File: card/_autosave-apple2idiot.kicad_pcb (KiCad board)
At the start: 2 copper layers, 167.6 x 77.5 mm, 4 parts, among them J1 CARD EDGE, U1 IDT7132, U2 ESP32-WROOM-32

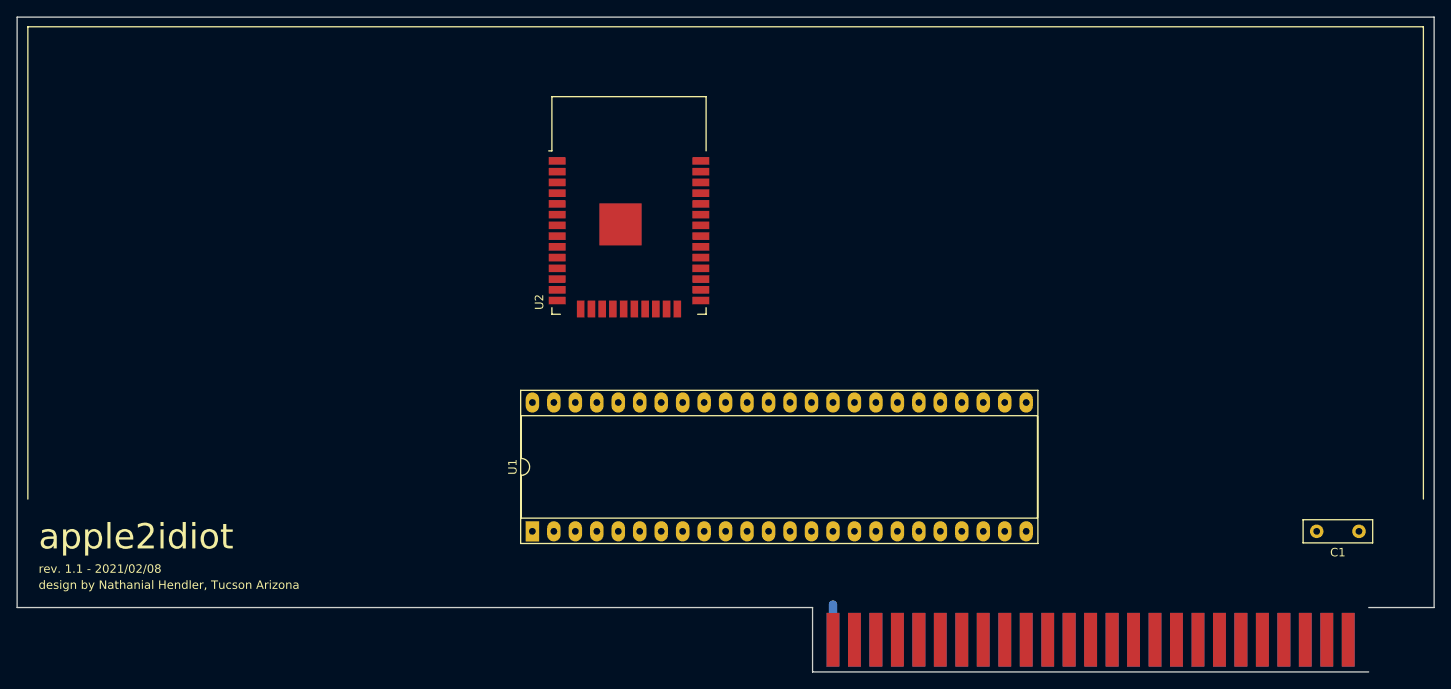
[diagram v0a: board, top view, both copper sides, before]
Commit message: ESP w/ webserver writes to RAM
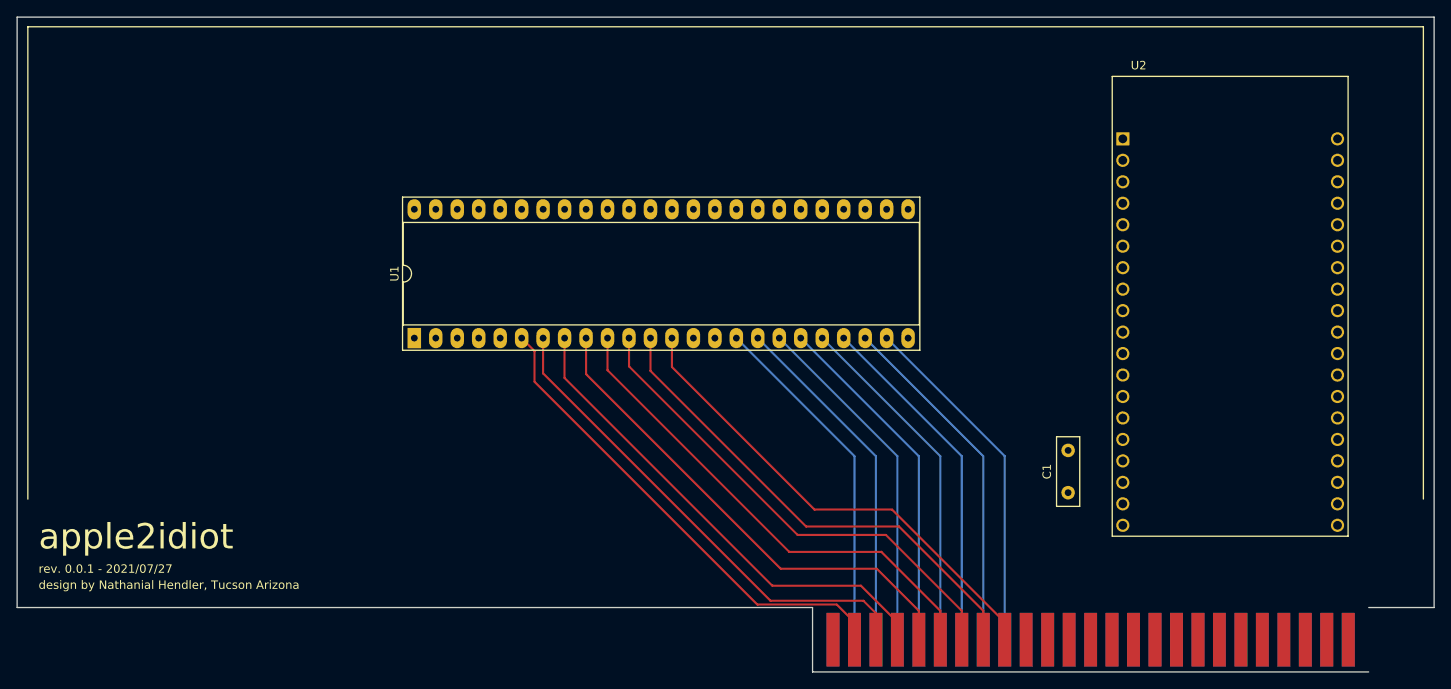
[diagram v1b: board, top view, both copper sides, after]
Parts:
- U2: value ESP32-WROOM-32 -> ESP32-DEVKITC-32D; footprint RF_Module:ESP32-WROOM-32 -> ESPDEVKIT:MODULE_ESP32-DEVKITC-32D
- moved U2 71.7 mm to (217.2, 88.9)
- moved C1 34.7 mm to (198.0, 111.0), turned to 90 degrees
- moved U1 26.8 mm to (120.7, 92.7)
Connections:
- U1 pad 25: /D7R -> Net-(U1-Pad25)
- U1 pad 26: /D6R -> Net-(U1-Pad26)
- U1 pad 27: /D5R -> Net-(U1-Pad27)
- U1 pad 28: /D4R -> Net-(U1-Pad28)
- U1 pad 29: /D3R -> Net-(U1-Pad29)
- U1 pad 30: /D2R -> Net-(U1-Pad30)
- U1 pad 31: /D1R -> Net-(U1-Pad31)
- U1 pad 32: /D0R -> Net-(U1-Pad32)
- U1 pad 48: VCC -> +5V
- U2 pad 1: GND -> Net-(U2-Pad1)
- U2 pad 10: Net-(U1-Pad41) -> Net-(U1-Pad40)
- U2 pad 11: Net-(U1-Pad40) -> Net-(U1-Pad39)
- U2 pad 12: Net-(U1-Pad39) -> Net-(U1-Pad27)
- U2 pad 13: Net-(U2-Pad13) -> Net-(U1-Pad25)
- U2 pad 14: Net-(U2-Pad14) -> GND
- U2 pad 15: GND -> Net-(U1-Pad26)
- U2 pad 19: Net-(U2-Pad19) -> +5V
- U2 pad 20: Net-(U2-Pad20) -> GND
- U2 pad 21: Net-(U2-Pad21) -> Net-(U1-Pad42)
- U2 pad 22: Net-(U2-Pad22) -> Net-(U1-Pad32)
- U2 pad 25: Net-(U2-Pad25) -> Net-(U1-Pad31)
- U2 pad 26: Net-(U1-Pad38) -> GND
- U2 pad 27: Net-(U2-Pad27) -> Net-(U1-Pad30)
- U2 pad 28: Net-(U2-Pad28) -> Net-(U1-Pad29)
- U2 pad 35: Net-(U2-Pad35) -> Net-(U1-Pad28)
- U2 pad 37: Net-(U1-Pad42) -> Net-(U2-Pad37)
- U2 pad 38: GND -> Net-(U2-Pad38)
- U2 pad 5: Net-(U2-Pad5) -> /~IOSEL
- U2 pad 6: Net-(U1-Pad45) -> Net-(U1-Pad3)
- U2 pad 7: Net-(U1-Pad3) -> Net-(U1-Pad38)
- U2 pad 8: Net-(U2-Pad8) -> Net-(U1-Pad37)
- U2 pad 9: /~IOSEL -> Net-(U1-Pad41)
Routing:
- net /A3: track 0.00 -> 58.7 mm
- net /A6: track 0.00 -> 58.4 mm
- net /A1: track 0.00 -> 58.4 mm
- net /A4: track 0.00 -> 58.4 mm
- net /A2: track 0.00 -> 58.1 mm
- net /A5: track 0.00 -> 58.1 mm
- net /A0: track 0.00 -> 57.5 mm
- net /A7: track 0.00 -> 57.4 mm
- net /D7: track 0.00 -> 41.5 mm
- net /D6: track 0.00 -> 41.5 mm
- net /D5: track 0.00 -> 41.5 mm
- net /D4: track 0.00 -> 41.5 mm
- net /D3: track 0.00 -> 41.5 mm
- net /D2: track 0.00 -> 41.5 mm
- net /D1: track 0.00 -> 41.5 mm
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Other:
- board text added: "rev. 0.0.1 - 2021/07/27"
- board text removed: "rev. 1.1 - 2021/02/08"
